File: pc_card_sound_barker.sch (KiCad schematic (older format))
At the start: 43 parts, among them IC1 MCP100-300D, IC2 74LVC1G00, IC3 MCP100-450D, IC4 TPA152DR, J1 IC1F-68RD-1.27SF(52), J2 Headphones Out, U1 Z8601720ASG, U2 25LCxxx, U3 YMF289B-S, U4 YAC516-E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

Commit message: BOM, tracks, cleanup
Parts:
- C11, C12, C13, C9: Mouser Part Number https://www.mouser.co.uk/ProductDetail/80-C0805C105M3RECLR -> 80-C0805C105M3RECLR
- JP1: symbol Device:Jumper_NO_Small -> Device:Jumper_NC_Small
- R10: Manufacturer_Name Panasonic -> (none); Manufacturer_Part_Number ERJ-XGNJ392Y -> (none); Mouser Part Number 667-ERJ-XGNJ392Y -> (none)
- R2, R9: Manufacturer_Name (none) -> Panasonic; Manufacturer_Part_Number (none) -> ERJ-U02F3901X; Mouser Part Number (none) -> 667-ERJ-U02F3901X
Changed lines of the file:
@@
 F 4 "KEMET" H 10300 5400 50  0001 C CNN "Manufacturer_Name"
 F 5 "C0805C105M3REC7210" H 10300 5400 50  0001 C CNN "Manufacturer_Part_Number"
-F 6 "https://www.mouser.co.uk/ProductDetail/80-C0805C105M3RECLR" H 10300 5400 50  0001 C CNN "Mouser Part Number"
+F 6 "80-C0805C105M3RECLR" H 10300 5400 50  0001 C CNN "Mouser Part Number"
 F 7 "https://www.mouser.co.uk/ProductDetail/80-C0805C105M3RECLR" H 10300 5400 50  0001 C CNN "Mouser Price/Stock"
 	1    10300 5400
@@
 F 4 "KEMET" H 8350 6100 50  0001 C CNN "Manufacturer_Name"
 F 5 "C0805C105M3REC7210" H 8350 6100 50  0001 C CNN "Manufacturer_Part_Number"
-F 6 "https://www.mouser.co.uk/ProductDetail/80-C0805C105M3RECLR" H 8350 6100 50  0001 C CNN "Mouser Part Number"
+F 6 "80-C0805C105M3RECLR" H 8350 6100 50  0001 C CNN "Mouser Part Number"
 F 7 "https://www.mouser.co.uk/ProductDetail/80-C0805C105M3RECLR" H 8350 6100 50  0001 C CNN "Mouser Price/Stock"
 	1    8350 6100
@@
 F 4 "KEMET" H 8500 5550 50  0001 C CNN "Manufacturer_Name"
 F 5 "C0805C105M3REC7210" H 8500 5550 50  0001 C CNN "Manufacturer_Part_Number"
-F 6 "https://www.mouser.co.uk/ProductDetail/80-C0805C105M3RECLR" H 8500 5550 50  0001 C CNN "Mouser Part Number"
+F 6 "80-C0805C105M3RECLR" H 8500 5550 50  0001 C CNN "Mouser Part Number"
 F 7 "https://www.mouser.co.uk/ProductDetail/80-C0805C105M3RECLR" H 8500 5550 50  0001 C CNN "Mouser Price/Stock"
 	1    8500 5550
@@
 F 4 "KEMET" H 10350 4900 50  0001 C CNN "Manufacturer_Name"
 F 5 "C0805C105M3REC7210" H 10350 4900 50  0001 C CNN "Manufacturer_Part_Number"
-F 6 "https://www.mouser.co.uk/ProductDetail/80-C0805C105M3RECLR" H 10350 4900 50  0001 C CNN "Mouser Part Number"
+F 6 "80-C0805C105M3RECLR" H 10350 4900 50  0001 C CNN "Mouser Part Number"
 F 7 "https://www.mouser.co.uk/ProductDetail/80-C0805C105M3RECLR" H 10350 4900 50  0001 C CNN "Mouser Price/Stock"
 	1    10350 4900
@@
 F 1 "100" H 8130 5095 50  0000 R CNN
 F 2 "Resistor_SMD:R_1206_3216Metric_Pad1.30x1.75mm_HandSolder" V 8130 5050 50  0001 C CNN
-F 3 "~" H 8200 5050 50  0001 C CNN
+F 3 "https://www.mouser.co.uk/datasheet/2/315/AOA0000C334-1314047.pdf" H 8200 5050 50  0001 C CNN
+F 4 "Panasonic" H 8200 5050 50  0001 C CNN "Manufacturer_Name"
+F 5 "ERJ-U02F3901X" H 8200 5050 50  0001 C CNN "Manufacturer_Part_Number"
+F 6 "667-ERJ-U02F3901X" H 8200 5050 50  0001 C CNN "Mouser Part Number"
 	1    8200 5050
 	1    0    0    -1
@@
 F 1 "100" H 10480 5945 50  0000 R CNN
 F 2 "Resistor_SMD:R_1206_3216Metric_Pad1.30x1.75mm_HandSolder" V 10480 5900 50  0001 C CNN
-F 3 "~" H 10550 5900 50  0001 C CNN
+F 3 "https://www.mouser.co.uk/datasheet/2/315/AOA0000C334-1314047.pdf" H 10550 5900 50  0001 C CNN
+F 4 "Panasonic" H 10550 5900 50  0001 C CNN "Manufacturer_Name"
+F 5 "ERJ-U02F3901X" H 10550 5900 50  0001 C CNN "Manufacturer_Part_Number"
+F 6 "667-ERJ-U02F3901X" H 10550 5900 50  0001 C CNN "Mouser Part Number"
 	1    10550 5900
 	-1   0    0    1
@@
 Text GLabel 6550 1850 3    50   UnSpc ~ 0
 GNDD
-$Comp
-L Device:Jumper_NO_Small JP1
-U 1 1 61998785
-P 6450 1750
-F 0 "JP1" H 6450 1935 50  0000 C CNN
-F 1 "3.3V" H 6450 1844 50  0000 C CNN
-F 2 "Jumper:SolderJumper-2_P1.3mm_Bridged_RoundedPad1.0x1.5mm" H 6450 1750 50  0001 C CNN
-F 3 "~" H 6450 1750 50  0001 C CNN
-	1    6450 1750
-	1    0    0    -1
-$EndComp
 Text GLabel 6100 1850 2    50   Output ~ 0
 IORD#
@@
 F 1 "3.9k" V 7316 3050 50  0000 C CNN
 F 2 "Resistor_SMD:R_0402_1005Metric_Pad0.72x0.64mm_HandSolder" V 7130 3050 50  0001 C CNN
-F 3 "https://www.mouser.co.uk/datasheet/2/315/AOA0000C301-1488782.pdf" H 7200 3050 50  0001 C CNN
-F 4 "ERJ-XGNJ392Y" H 7200 3050 50  0001 C CNN "Manufacturer_Part_Number"
-F 5 "667-ERJ-XGNJ392Y" H 7200 3050 50  0001 C CNN "Mouser Part Number"
+F 3 "" H 7200 3050 50  0001 C CNN
+F 4 "" H 7200 3050 50  0001 C CNN "Manufacturer_Part_Number"
+F 5 "" H 7200 3050 50  0001 C CNN "Mouser Part Number"
 F 6 "https://www.mouser.co.uk/ProductDetail/667-ERJ-XGNJ392Y" H 7200 3050 50  0001 C CNN "Mouser Price/Stock"
-F 7 "Panasonic" H 7200 3050 50  0001 C CNN "Manufacturer_Name"
+F 7 "" H 7200 3050 50  0001 C CNN "Manufacturer_Name"
 	1    7200 3050
 	-1   0    0    1
@@
 Text Notes 10550 7650 0    50   ~ 0
 Prototype One
+$Comp
+L Device:Jumper_NC_Small JP1
+U 1 1 61998785
+P 6450 1750
+F 0 "JP1" H 6450 1935 50  0000 C CNN
+F 1 "3.3V" H 6450 1844 50  0000 C CNN
+F 2 "Jumper:SolderJumper-2_P1.3mm_Bridged_RoundedPad1.0x1.5mm" H 6450 1750 50  0001 C CNN
+F 3 "~" H 6450 1750 50  0001 C CNN
+	1    6450 1750
+	1    0    0    -1
+$EndComp
 $EndSCHEMATC

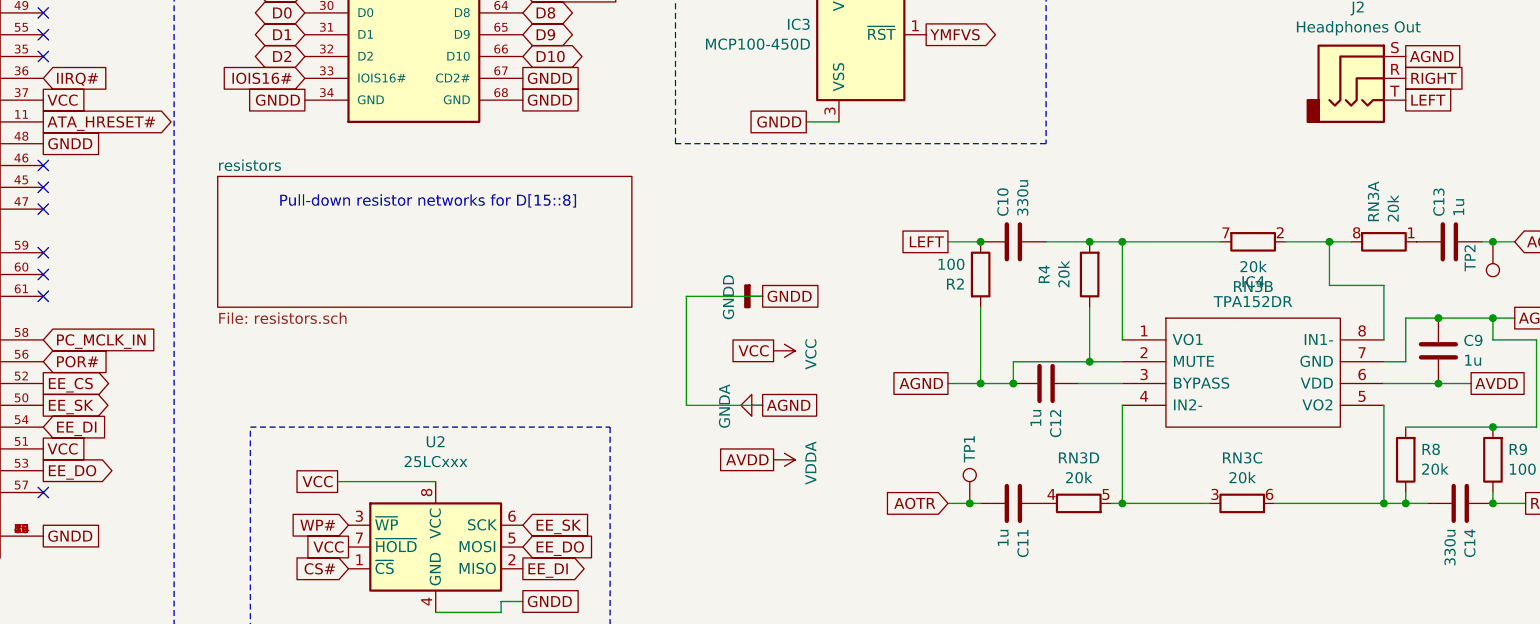
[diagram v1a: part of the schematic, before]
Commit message: remove pull-downs for unused address lines
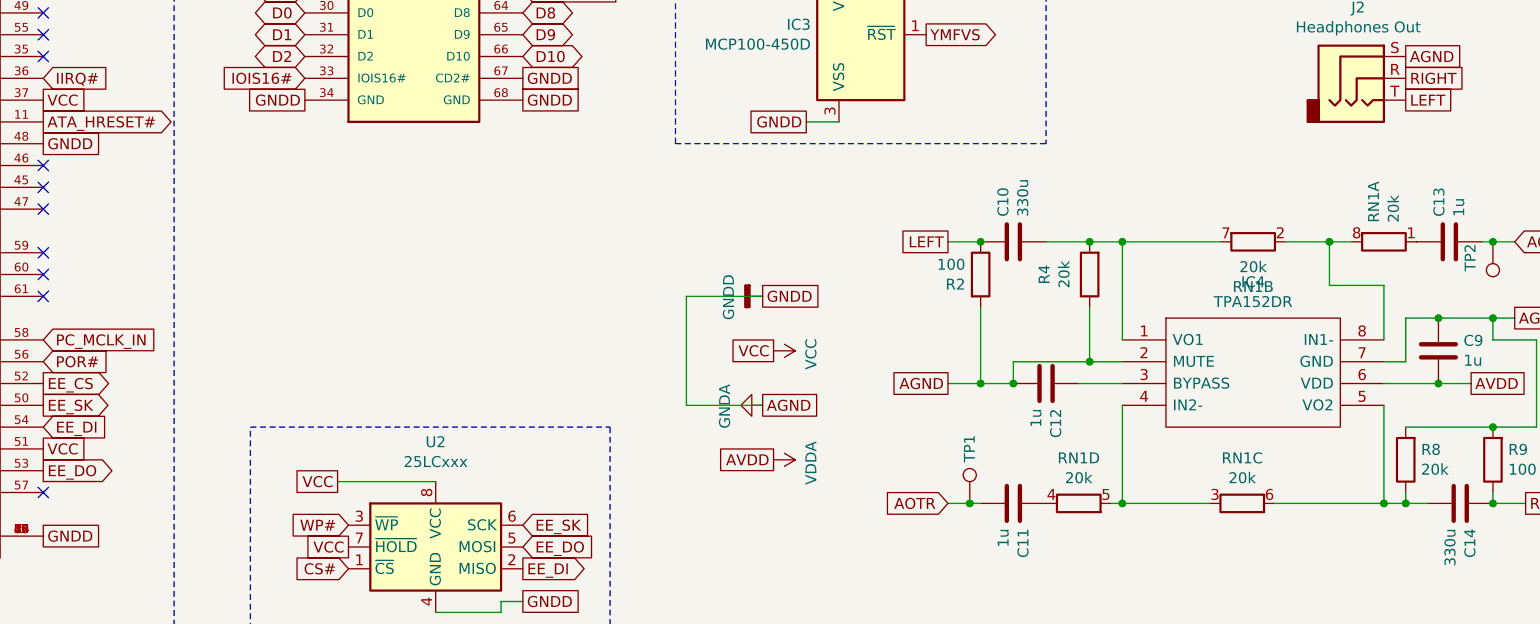
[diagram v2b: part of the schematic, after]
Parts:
- renumbered RN3 to RN1
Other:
- note removed: "Pull-down resistor networks for D[15::8]"
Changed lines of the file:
@@
 $Descr A4 11693 8268
 encoding utf-8
-Sheet 1 2
+Sheet 1 1
 Title ""
 Date ""
@@
 Text GLabel 6100 3050 2    50   UnSpc ~ 0
 A25
-$Sheet
-S 4700 4600 1900 600
-U 61F03A72
-F0 "resistors" 50
-F1 "resistors.sch" 50
-$EndSheet
-Text Notes 6350 4750 2    50   ~ 0
-Pull-down resistor networks for D[15::8]
 Wire Notes Line
 	4500 600  4500 7550
@@
 VCC
 $Comp
-L Device:R_Pack04_Split RN3
+L Device:R_Pack04_Split RN1
 U 1 1 61A465A5
 P 10050 4900
-F 0 "RN3" H 10138 4946 50  0000 L CNN
+F 0 "RN1" H 10138 4946 50  0000 L CNN
 F 1 "20k" H 10138 4855 50  0000 L CNN
 F 2 "Resistor_SMD:R_Array_Convex_4x1206" V 9970 4900 50  0001 C CNN
@@
 $EndComp
 $Comp
-L Device:R_Pack04_Split RN3
+L Device:R_Pack04_Split RN1
 U 2 1 61A5660A
 P 9450 4900
-F 0 "RN3" V 9243 4900 50  0000 C CNN
+F 0 "RN1" V 9243 4900 50  0000 C CNN
 F 1 "20k" V 9334 4900 50  0000 C CNN
 F 2 "Resistor_SMD:R_Array_Convex_4x1206" V 9370 4900 50  0001 C CNN
@@
 $EndComp
 $Comp
-L Device:R_Pack04_Split RN3
+L Device:R_Pack04_Split RN1
 U 3 1 61A630DD
 P 9400 6100
-F 0 "RN3" V 9193 6100 50  0000 C CNN
+F 0 "RN1" V 9193 6100 50  0000 C CNN
 F 1 "20k" V 9284 6100 50  0000 C CNN
 F 2 "Resistor_SMD:R_Array_Convex_4x1206" V 9320 6100 50  0001 C CNN
@@
 $EndComp
 $Comp
-L Device:R_Pack04_Split RN3
+L Device:R_Pack04_Split RN1
 U 4 1 61A641E1
 P 8650 6100
-F 0 "RN3" V 8443 6100 50  0000 C CNN
+F 0 "RN1" V 8443 6100 50  0000 C CNN
 F 1 "20k" V 8534 6100 50  0000 C CNN
 F 2 "Resistor_SMD:R_Array_Convex_4x1206" V 8570 6100 50  0001 C CNN
